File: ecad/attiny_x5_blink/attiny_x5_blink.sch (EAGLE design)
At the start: 3 parts

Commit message: Update gitignore.  Modify schematic and code to fix pins and update device meta data.
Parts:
- R: device PiB_resistors:10KΩ_PTH-0207/7_1/8W-5% -> PiB_resistors:10KΩ_PTH-207/7_1/4W-5%
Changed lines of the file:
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@@
 <setting verticaltext="up"/>
 </settings>
-<grid distance="0.1" unitdist="inch" unit="inch" style="lines" multiple="1" display="yes" altdistance="0.01" altunitdist="inch" altunit="inch"/>
+<grid distance="0.1" unitdist="inch" unit="inch" style="lines" multiple="1" display="no" altdistance="0.01" altunitdist="inch" altunit="inch"/>
 <layers>
 <layer number="1" name="Top" color="4" fill="1" visible="no" active="no"/>
@@
 </part>
 <part name="LED" library="PiB_leds" deviceset="LED" device="_PTH-5MM_NO-COLOR"/>
-<part name="R" library="PiB_resistors" deviceset="10KΩ" device="_PTH-0207/7_1/8W-5%" package3d_urn="urn:adsk.eagle:package:2749854/2" value="10K"/>
+<part name="R" library="PiB_resistors" deviceset="10KΩ" device="_PTH-207/7_1/4W-5%" package3d_urn="urn:adsk.eagle:package:4254576/1" value="10K"/>
 <part name="SUPPLY2" library="PiB_power_symbols" deviceset="GND" device=""/>
 </parts>

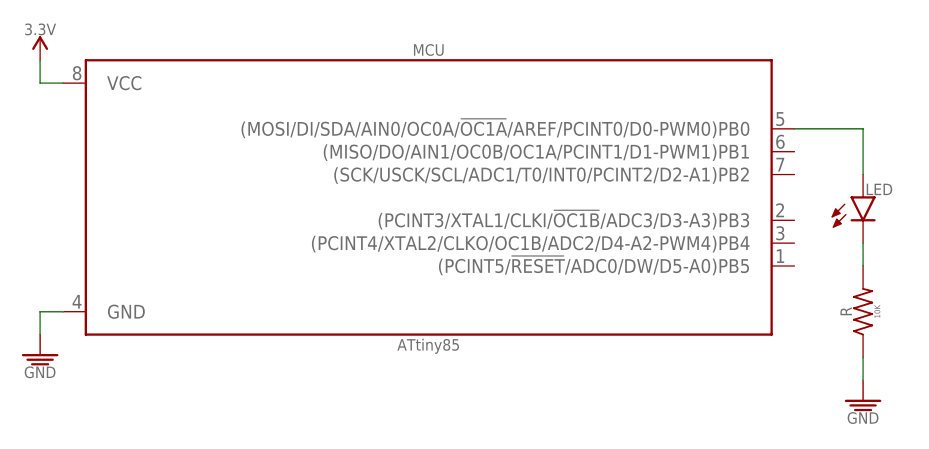
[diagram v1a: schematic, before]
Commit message: Create schematic for pocket avr programmer (AVR ISP header) to ATtiny85.  Updated all schematics and their respective images.
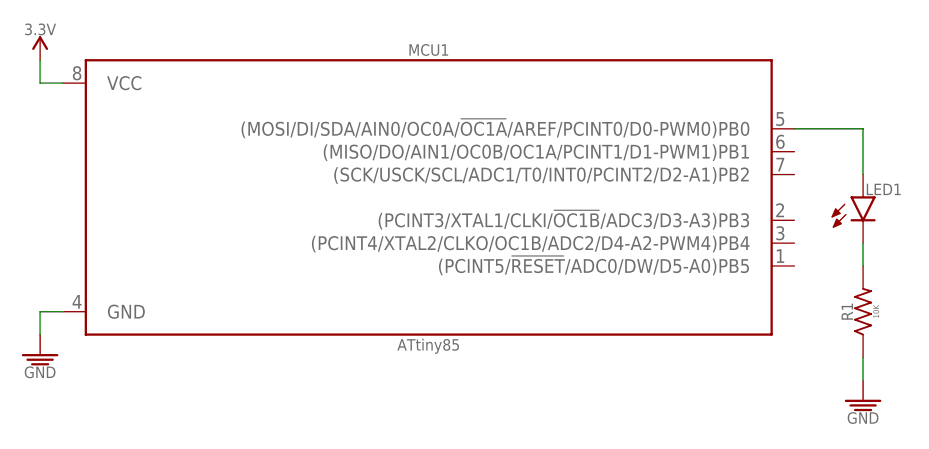
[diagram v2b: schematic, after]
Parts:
- removed LED: (no value), PiB_leds:LED_PTH-5MM_NO-COLOR
- removed R: 10K, PiB_resistors:10KΩ_PTH-207/7_1/4W-5%
- added LED1: (no value), PiB_leds:LED_PTH_T-1_3/4_5MM_NO-COLOR
- added R1: 10K, PiB_resistors:10KΩ_PTH-207/10_1/4W-5%
- renumbered MCU to MCU1
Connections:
- net GND: now also R1.1; no longer R.1
- net N$1: now also LED1.A; no longer LED.A
- net N$2: now also LED1.K, R1.2; no longer LED.K, R.2
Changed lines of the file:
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@@
 <?xml version="1.0" encoding="utf-8"?>
 <!DOCTYPE eagle SYSTEM "eagle.dtd">
-<eagle version="9.1.1">
+<eagle version="9.1.3">
 <drawing>
 <settings>
@@
 </classes>
 <parts>
-<part name="MCU" library="PiB_ic_microcontrollers" deviceset="ATTINY-X5" device="_DIP-8_ATTINY-85" package3d_urn="urn:adsk.eagle:package:3650792/3" value="ATtiny85">
+<part name="MCU1" library="PiB_ic_microcontrollers" deviceset="ATTINY-X5" device="_DIP-8_ATTINY-85" package3d_urn="urn:adsk.eagle:package:3650792/3" value="ATtiny85">
 <attribute name="SPICEPREFIX" value="X"/>
 </part>
@@
 <attribute name="SPICEPREFIX" value="G"/>
 </part>
-<part name="LED" library="PiB_leds" deviceset="LED" device="_PTH-5MM_NO-COLOR"/>
-<part name="R" library="PiB_resistors" deviceset="10KΩ" device="_PTH-207/7_1/4W-5%" package3d_urn="urn:adsk.eagle:package:4254576/1" value="10K"/>
+<part name="LED1" library="PiB_leds" deviceset="LED" device="_PTH_T-1_3/4_5MM_NO-COLOR" package3d_urn="urn:adsk.eagle:package:4254847/2"/>
+<part name="R1" library="PiB_resistors" deviceset="10KΩ" device="_PTH-207/10_1/4W-5%" package3d_urn="urn:adsk.eagle:package:4254576/1" value="10K"/>
 <part name="SUPPLY2" library="PiB_power_symbols" deviceset="GND" device=""/>
 </parts>
@@
 </plain>
 <instances>
-<instance part="MCU" gate="G$1" x="50.8" y="30.48"/>
+<instance part="MCU1" gate="G$1" x="50.8" y="30.48"/>
 <instance part="SUPPLY1" gate="GND" x="7.62" y="12.7"/>
 <instance part="SUPPLY4" gate="3.3V" x="7.62" y="45.72"/>
-<instance part="LED" gate="G$1" x="99.06" y="30.48"/>
-<instance part="R" gate="G$1" x="99.06" y="17.78" rot="R90"/>
+<instance part="LED1" gate="G$1" x="99.06" y="30.48"/>
+<instance part="R1" gate="G$1" x="99.06" y="17.78" rot="R90"/>
 <instance part="SUPPLY2" gate="GND" x="99.06" y="7.62"/>
 </instances>
@@
 <segment>
 <wire x1="7.62" y1="15.24" x2="7.62" y2="17.78" width="0.1524" layer="91"/>
-<pinref part="MCU" gate="G$1" pin="GND"/>
+<pinref part="MCU1" gate="G$1" pin="GND"/>
 <wire x1="7.62" y1="17.78" x2="10.16" y2="17.78" width="0.1524" layer="91"/>
 <pinref part="SUPPLY1" gate="GND" pin="GND"/>
 </segment>
 <segment>
-<pinref part="R" gate="G$1" pin="1"/>
+<pinref part="R1" gate="G$1" pin="1"/>
 <pinref part="SUPPLY2" gate="GND" pin="GND"/>
 <wire x1="99.06" y1="10.16" x2="99.06" y2="12.7" width="0.1524" layer="91"/>
@@
 <net name="3.3V" class="0">
 <segment>
-<pinref part="MCU" gate="G$1" pin="VCC"/>
+<pinref part="MCU1" gate="G$1" pin="VCC"/>
 <wire x1="10.16" y1="43.18" x2="7.62" y2="43.18" width="0.1524" layer="91"/>
 <wire x1="7.62" y1="43.18" x2="7.62" y2="45.72" width="0.1524" layer="91"/>
@@
 <net name="N$1" class="0">
 <segment>
-<pinref part="MCU" gate="G$1" pin="(MOSI/DI/SDA/AIN0/OC0A/!OC1A!/AREF/PCINT0/D0-PWM0)PB0"/>
+<pinref part="MCU1" gate="G$1" pin="(MOSI/DI/SDA/AIN0/OC0A/!OC1A!/AREF/PCINT0/D0-PWM0)PB0"/>
 <wire x1="91.44" y1="38.1" x2="99.06" y2="38.1" width="0.1524" layer="91"/>
 <wire x1="99.06" y1="38.1" x2="99.06" y2="33.02" width="0.1524" layer="91"/>
-<pinref part="LED" gate="G$1" pin="A"/>
+<pinref part="LED1" gate="G$1" pin="A"/>
 </segment>
 </net>
 <net name="N$2" class="0">
 <segment>
-<pinref part="LED" gate="G$1" pin="K"/>
+<pinref part="LED1" gate="G$1" pin="K"/>
 <wire x1="99.06" y1="25.4" x2="99.06" y2="22.86" width="0.1524" layer="91"/>
-<pinref part="R" gate="G$1" pin="2"/>
-</segment>
-</net>
+<pinref part="R1" gate="G$1" pin="2"/>
+</segment>
+</net>
